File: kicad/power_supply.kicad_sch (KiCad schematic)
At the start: 14 parts, among them U2 LMR16030

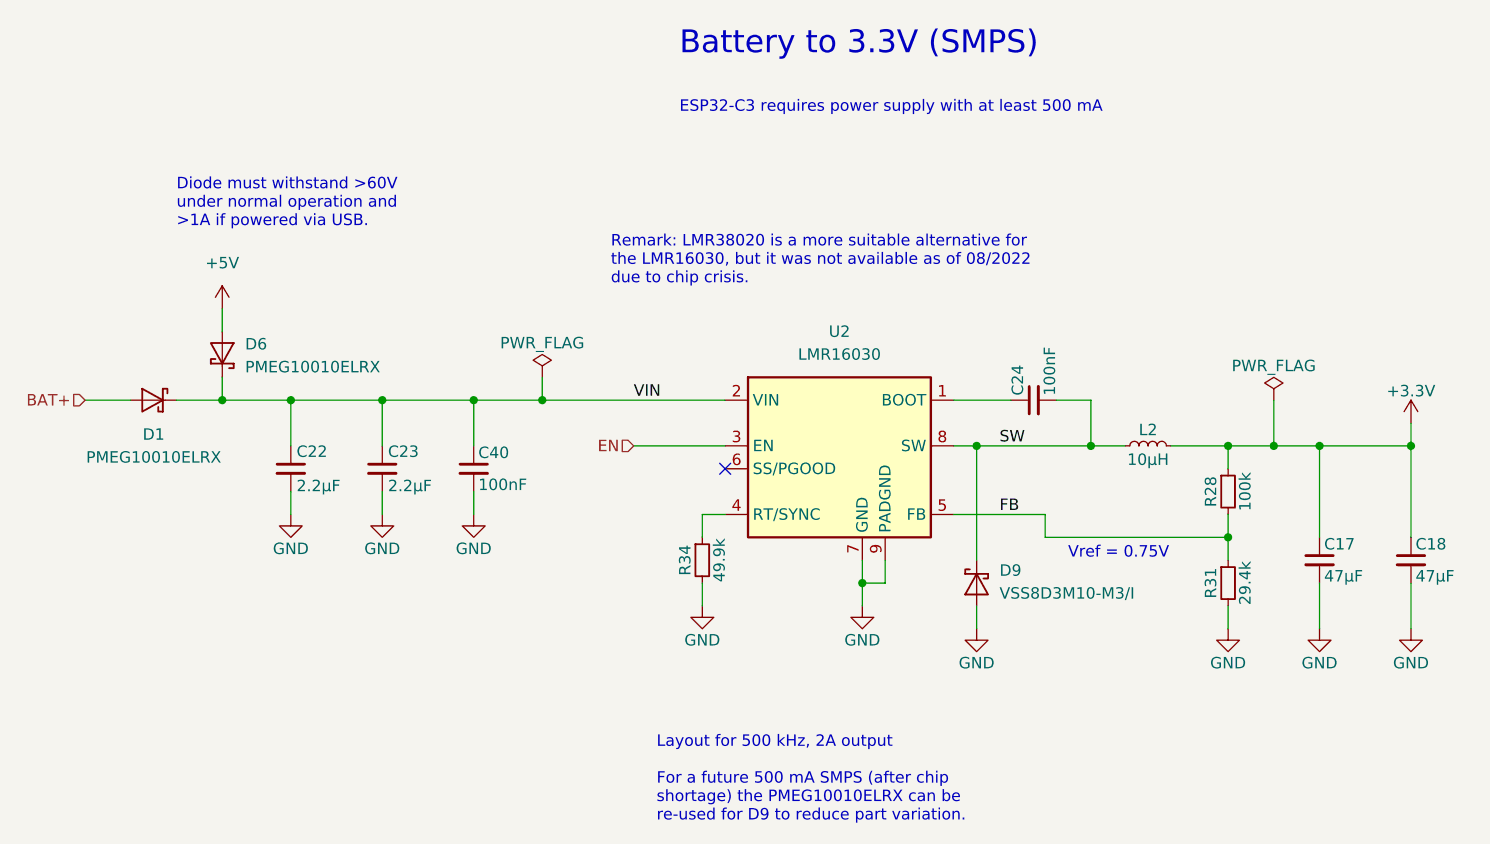
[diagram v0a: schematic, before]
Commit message: v0.4.0: Multiple improvements for new board revision
- Use LMR38010 for internal power supply (max. 80V instead of 60V)
- Change USB connector from Micro-A to C and remove 5V power supply
  which was not working anyway. The board cannot be powered by USB
  only.
- Add TS2 (connected to DFETOFF) to measure shunt temperature
- Add RS-485 transceiver (sharing the connector with CAN)
- Switch I2C pins of ESP32-C3 to GPIO8/9. This allows to re-use the
  I2C pull-ups for strapping configuration and frees two pins for the
  RS-485 transceiver RE and DE pins. Also we may get rid of the I2C
  glitches during start-up.
- Reduce DSG gate resistor R57 to 47R to increase switch-off speed.
- Use more easily available and cheaper Würth 7466005R terminals with
  countersunk hole/thread.
- Adjust some resistors to reduce number of different parts
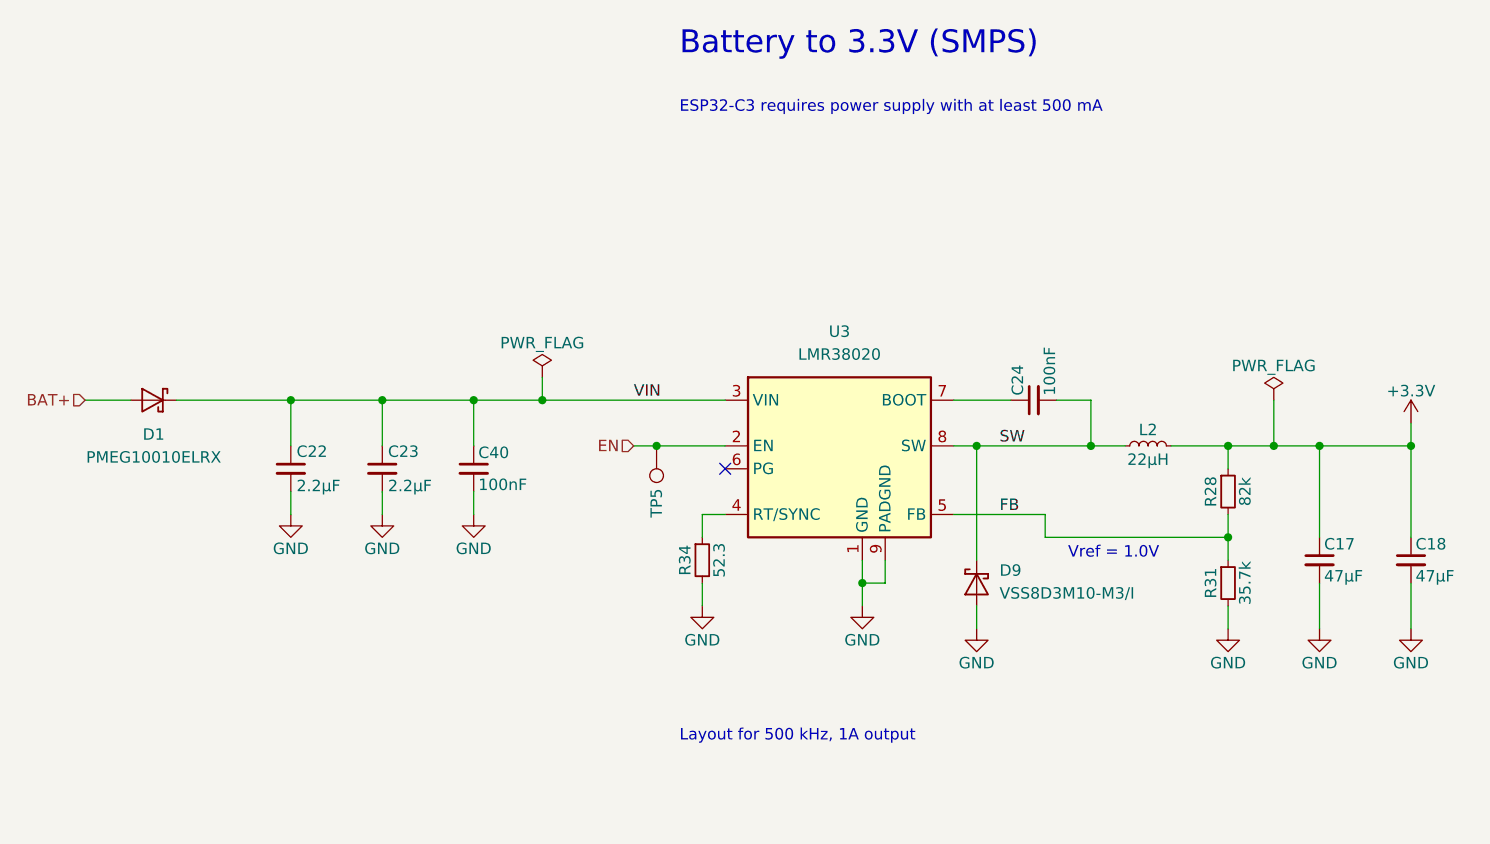
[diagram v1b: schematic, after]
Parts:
- removed D6: PMEG10010ELRX, LibreSolar:D_SOD-123F, symbol LibreSolar:D_Schottky
- removed U2: LMR16030, Package_SO:SOIC-8-1EP_3.9x4.9mm_P1.27mm_EP2.29x3mm, symbol LibreSolar:LMR16030
- added TP5: TestPoint, TestPoint:TestPoint_Pad_D1.5mm, symbol Connector:TestPoint
- added U3: LMR38020, LibreSolar:SOIC-8-1EP_3.9x4.9mm_P1.27mm_EP2.4x3.1mm_ThermalVias, symbol LibreSolar:LMR38020
- L2: value 10µH -> 22µH
- R28: value 100k -> 82k
- R31: value 29.4k -> 35.7k
- R34: value 49.9k -> 52.3
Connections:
- net EN: now also TP5.1, U3.2 (EN)
- net FB: now also U3.5 (FB)
- net GND: now also U3.1 (GND), U3.9 (PADGND)
- net SW: now also U3.8 (SW)
- net VIN: now also U3.3 (VIN)
- net at C24.1: now also U3.7 (BOOT)
- net at R34.1: now also U3.4 (RT/SYNC)
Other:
- note added: "Layout for 500 kHz, 1A output"
- note added: "Vref = 1.0V"
- note removed: "Diode must withstand >60V under normal operation and >1A if powered via USB."
- note removed: "Layout for 500 kHz, 2A output For a future 500 mA SMPS (after chip shortage) the PMEG10010ELRX can be re-used for D9 to reduce part variation."
- note removed: "Remark: LMR38020 is a more suitable alternative for the LMR16030, but it was not available as of 08/2022 due to chip crisis."
- note removed: "Vref = 0.75V"
